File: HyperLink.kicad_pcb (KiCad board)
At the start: 2 copper layers, 35 x 24 mm, 45 parts, among them J1 USB_C_Receptacle_USB2.0, J2 Conn_02x05_Odd_Even, J3 Conn_02x05_Odd_Even, SW1 SW_Push, U1 ESP32-C3, U2 PESD2USB5UXT, U3 MIC5504-3.3YM5, Y1 ABM11W-40.0000MHZ-8-B1U-T3

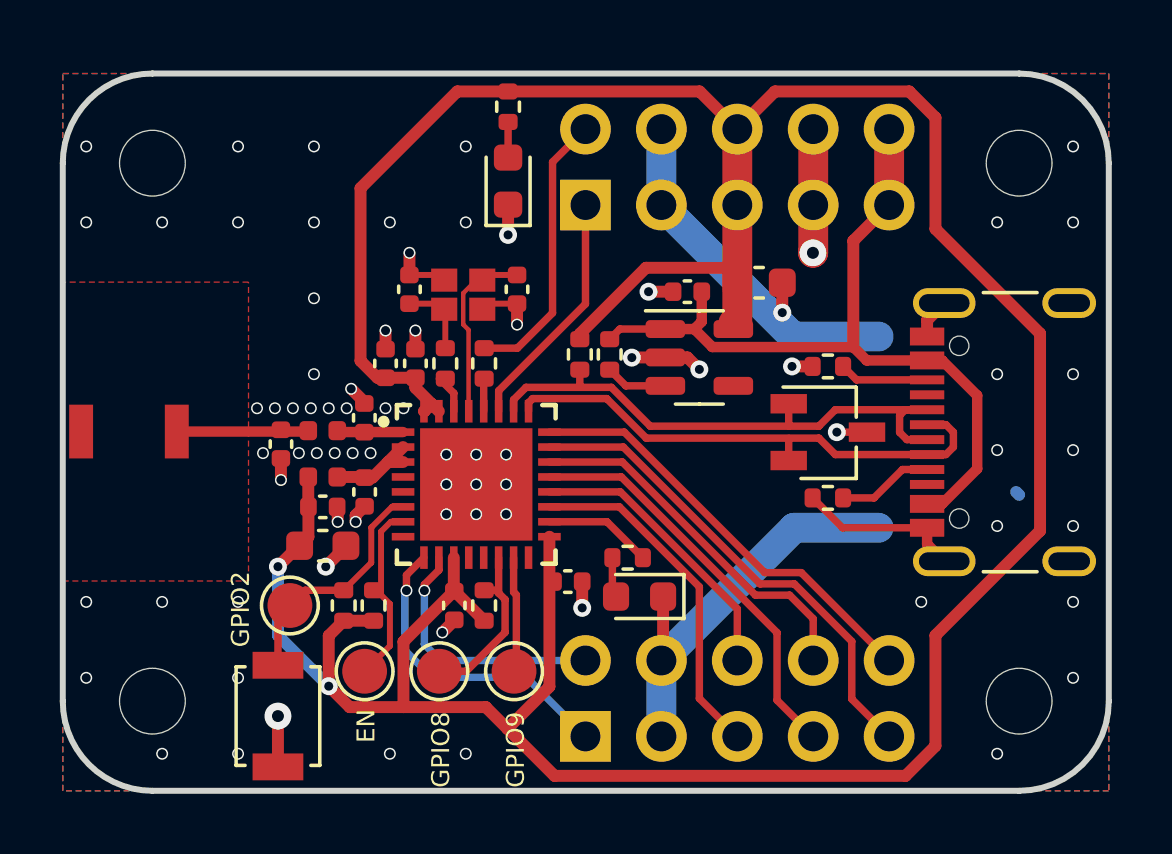
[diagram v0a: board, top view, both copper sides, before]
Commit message: Update crystal footprint
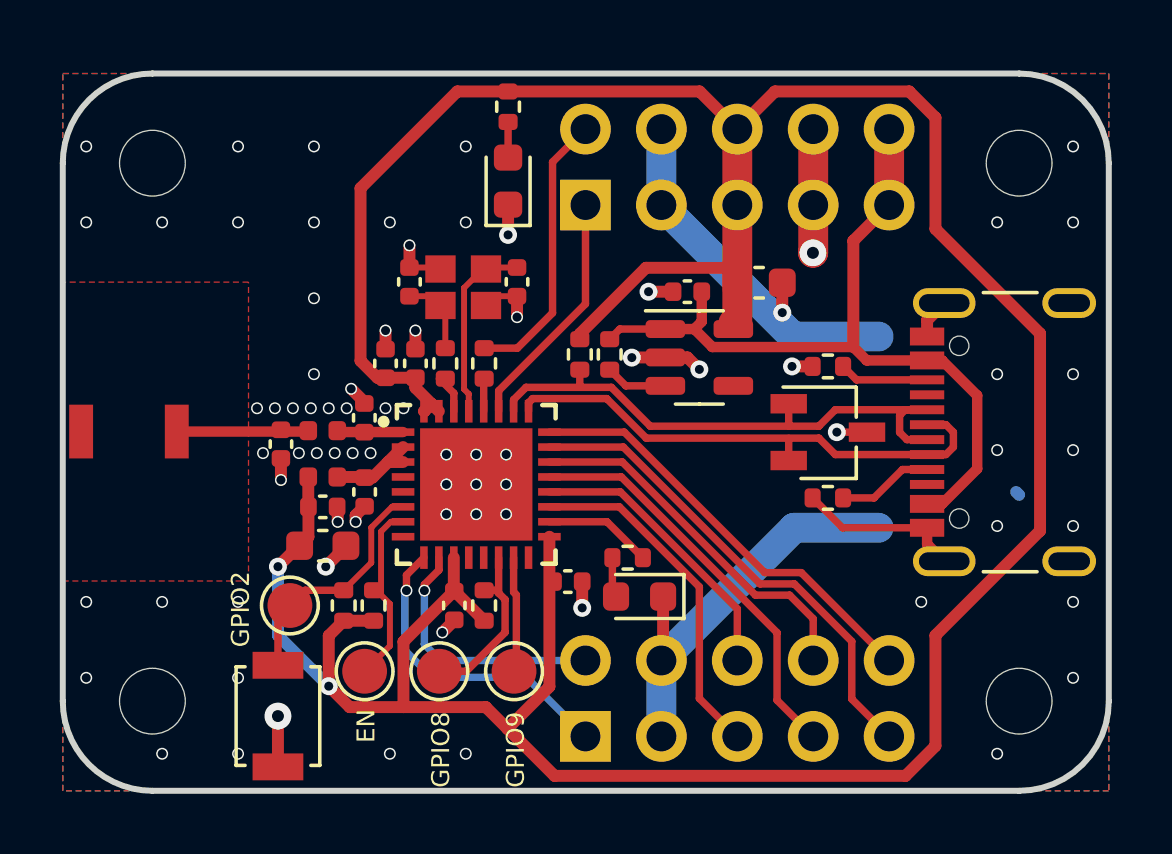
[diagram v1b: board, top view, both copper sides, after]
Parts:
- moved Y1 0.25 mm to (132.4, 77.2)
- moved C5 0.25 mm to (130.6, 77.0)
- moved C6 0.25 mm to (134.2, 77.0)
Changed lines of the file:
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@@
   )
   (footprint "Capacitor_SMD:C_0402_1005Metric" (layer "F.Cu")
-    (at 130.6 77.22 90)
+    (at 130.6 76.970999 90)
     (descr "Capacitor SMD 0402 (1005 Metric), square (rectangular) end terminal, IPC_7351 nominal, (Body size source: IPC-SM-782 page 76, https://www.pcb-3d.com/wordpress/wp-content/uploads/ipc-sm-782a_amendment_1_and_2.pdf), generated with kicad-footprint-generator")
     (tags "capacitor")
@@
   )
   (footprint "Capacitor_SMD:C_0402_1005Metric" (layer "F.Cu")
-    (at 134.2 77.22 -90)
+    (at 134.2 76.970999 -90)
     (descr "Capacitor SMD 0402 (1005 Metric), square (rectangular) end terminal, IPC_7351 nominal, (Body size source: IPC-SM-782 page 76, https://www.pcb-3d.com/wordpress/wp-content/uploads/ipc-sm-782a_amendment_1_and_2.pdf), generated with kicad-footprint-generator")
     (tags "capacitor")
@@
   )
   (footprint "encyclopedia_galactica:ABM11W-30.0000MHZ-7-D1X-T3" (layer "F.Cu")
-    (at 132.400001 77.4 180)
+    (at 132.400001 77.150999 180)
     (property "Sheetfile" "HyperLink.kicad_sch")
     (property "Sheetname" "")
     (property "ki_description" "Four pin crystal, GND on pins 2 and 3")
     (property "ki_keywords" "quartz ceramic resonator oscillator")
-    (clearance 0.1)
     (attr smd)
     (fp_text reference "Y1" (at 2.05 -2.16) (layer "F.SilkS") hide
@@
     (fp_line (start 1 -0.8) (end 1 0.8)
       (stroke (width 0.127) (type solid)) (layer "F.Fab"))
-    (pad "1" smd rect (at -0.637 -0.487 270) (size 0.775 0.875) (layers "F.Cu" "F.Paste" "F.Mask")
+    (pad "1" smd rect (at -0.762 -0.6096 270) (size 0.9144 1.016) (layers "F.Cu" "F.Paste" "F.Mask")
       (net 5 "GND") (pinfunction "1") (pintype "passive"))
-    (pad "2" smd rect (at 0.637 -0.487 270) (size 0.775 0.875) (layers "F.Cu" "F.Paste" "F.Mask")
+    (pad "2" smd rect (at 0.762 -0.6096 270) (size 0.9144 1.016) (layers "F.Cu" "F.Paste" "F.Mask")
       (net 20 "/XTAL_P") (pinfunction "2") (pintype "passive"))
-    (pad "3" smd rect (at -0.637 0.487 270) (size 0.775 0.875) (layers "F.Cu" "F.Paste" "F.Mask")
+    (pad "3" smd rect (at -0.762 0.6096 270) (size 0.9144 1.016) (layers "F.Cu" "F.Paste" "F.Mask")
       (net 21 "/XTAL_N") (pinfunction "3") (pintype "passive"))
-    (pad "4" smd rect (at 0.637 0.487 270) (size 0.775 0.875) (layers "F.Cu" "F.Paste" "F.Mask")
+    (pad "4" smd rect (at 0.762 0.6096 270) (size 0.9144 1.016) (layers "F.Cu" "F.Paste" "F.Mask")
       (net 5 "GND") (pinfunction "4") (pintype "passive"))
     (model "${KIPRJMOD}/encyclopedia_galactica/models/ABM11W-30.0000MHZ-7-D1X-T3.step"
@@
   (segment (start 128.2 84.52) (end 128.18 84.5) (width 0.4) (layer "F.Cu") (net 5))
   (segment (start 144.11 74.4) (end 144.11 71.86) (width 1) (layer "F.Cu") (net 5))
-  (segment (start 131.590001 76.74) (end 131.763001 76.913) (width 0.2) (layer "F.Cu") (net 5))
-  (segment (start 130.6 76.74) (end 131.590001 76.74) (width 0.2) (layer "F.Cu") (net 5))
+  (segment (start 131.590001 76.490999) (end 131.763001 76.663999) (width 0.2) (layer "F.Cu") (net 5))
+  (segment (start 130.6 76.490999) (end 131.590001 76.490999) (width 0.2) (layer "F.Cu") (net 5))
   (segment (start 143.075 78) (end 143.075 77) (width 0.4) (layer "F.Cu") (net 5))
   (segment (start 129.8 79.22) (end 129.8 78.6) (width 0.4) (layer "F.Cu") (net 5))
@@
   (segment (start 139.0875 87.5) (end 139.0875 89.5825) (width 0.4) (layer "F.Cu") (net 5))
   (segment (start 138.046557 79.5) (end 139.1625 79.5) (width 0.4) (layer "F.Cu") (net 5))
-  (segment (start 133.224001 77.7) (end 133.037001 77.887) (width 0.2) (layer "F.Cu") (net 5))
+  (segment (start 133.224001 77.450999) (end 133.037001 77.637999) (width 0.2) (layer "F.Cu") (net 5))
   (segment (start 139.0875 89.5825) (end 139.03 89.64) (width 0.4) (layer "F.Cu") (net 5))
   (segment (start 139.9 79.5) (end 139.1625 79.5) (width 0.4) (layer "F.Cu") (net 5))
   (segment (start 145.09 85.2) (end 147.92 85.2) (width 0.25) (layer "F.Cu") (net 5))
   (segment (start 128.475 85.825) (end 128.475 85.8) (width 0.4) (layer "F.Cu") (net 5))
-  (segment (start 134.2 78.4) (end 134.2 77.7) (width 0.4) (layer "F.Cu") (net 5))
+  (segment (start 134.2 78.150999) (end 134.2 77.450999) (width 0.4) (layer "F.Cu") (net 5))
   (segment (start 140.3 79.9) (end 139.9 79.5) (width 0.4) (layer "F.Cu") (net 5))
   (segment (start 136.38 87.88) (end 136.38 87) (width 0.4) (layer "F.Cu") (net 5))
-  (segment (start 130.6 76) (end 130.6 76.7) (width 0.4) (layer "F.Cu") (net 5))
+  (segment (start 130.6 75.750999) (end 130.6 76.450999) (width 0.4) (layer "F.Cu") (net 5))
   (segment (start 126.3 82.88) (end 126.3 83.6) (width 0.4) (layer "F.Cu") (net 5))
   (segment (start 127.8 86.5) (end 128.475 85.825) (width 0.4) (layer "F.Cu") (net 5))
   (segment (start 147.92 78.255) (end 148.495 77.68) (width 0.4) (layer "F.Cu") (net 5))
-  (segment (start 134.2 77.7) (end 133.224001 77.7) (width 0.2) (layer "F.Cu") (net 5))
+  (segment (start 134.2 77.450999) (end 133.224001 77.450999) (width 0.2) (layer "F.Cu") (net 5))
   (segment (start 138.040639 79.505918) (end 138.046557 79.5) (width 0.4) (layer "F.Cu") (net 5))
   (segment (start 144.11 74.4) (end 144.11 75.99) (width 1) (layer "F.Cu") (net 5))
@@
   (via (at 133.834851 84.7487) (size 0.4) (drill 0.3) (layers "F.Cu" "B.Cu") (net 5))
   (via (at 126.7 81.2) (size 0.4) (drill 0.3) (layers "F.Cu" "B.Cu") (free) (net 5))
-  (via (at 134.2 78.4) (size 0.4) (drill 0.3) (layers "F.Cu" "B.Cu") (free) (net 5))
+  (via (at 134.2 78.150999) (size 0.4) (drill 0.3) (layers "F.Cu" "B.Cu") (free) (net 5))
   (via (at 132.834851 83.7487) (size 0.4) (drill 0.3) (layers "F.Cu" "B.Cu") (net 5))
   (via (at 131.834851 84.7487) (size 0.4) (drill 0.3) (layers "F.Cu" "B.Cu") (net 5))
@@
   (via (at 132.834851 82.7487) (size 0.4) (drill 0.3) (layers "F.Cu" "B.Cu") (net 5))
   (via (at 124.865 74.979999) (size 0.4) (drill 0.3) (layers "F.Cu" "B.Cu") (free) (net 5))
-  (via (at 130.6 76) (size 0.4) (drill 0.3) (layers "F.Cu" "B.Cu") (free) (net 5))
+  (via (at 130.6 75.750999) (size 0.4) (drill 0.3) (layers "F.Cu" "B.Cu") (free) (net 5))
   (via (at 150.265 74.979999) (size 0.4) (drill 0.3) (layers "F.Cu" "B.Cu") (free) (net 5))
   (via (at 124.865 87.679999) (size 0.4) (drill 0.3) (layers "F.Cu" "B.Cu") (free) (net 5))
@@
   (segment (start 132.5 90) (end 133.8 88.7) (width 0.25) (layer "F.Cu") (net 19))
   (segment (start 133.8 87.6) (end 133.584852 87.384852) (width 0.25) (layer "F.Cu") (net 19))
-  (segment (start 131.8 79.19) (end 131.8 77.923999) (width 0.2) (layer "F.Cu") (net 20))
-  (segment (start 130.6 77.7) (end 131.576001 77.7) (width 0.2) (layer "F.Cu") (net 20))
-  (segment (start 131.576001 77.7) (end 131.763001 77.887) (width 0.2) (layer "F.Cu") (net 20))
-  (segment (start 131.8 77.923999) (end 131.763001 77.887) (width 0.2) (layer "F.Cu") (net 20))
-  (segment (start 134.2 76.74) (end 133.210001 76.74) (width 0.2) (layer "F.Cu") (net 21))
-  (segment (start 132.578 78.578) (end 132.4 78.4) (width 0.15) (layer "F.Cu") (net 21))
-  (segment (start 133.210001 76.74) (end 133.037001 76.913) (width 0.2) (layer "F.Cu") (net 21))
-  (segment (start 132.4 77.349001) (end 132.836001 76.913) (width 0.15) (layer "F.Cu") (net 21))
-  (segment (start 132.836001 76.913) (end 133.037001 76.913) (width 0.15) (layer "F.Cu") (net 21))
-  (segment (start 132.4 78.4) (end 132.4 77.349001) (width 0.15) (layer "F.Cu") (net 21))
-  (segment (start 132.584851 81.3) (end 132.578 81.293149) (width 0.15) (layer "F.Cu") (net 21))
-  (segment (start 132.578 81.293149) (end 132.578 78.578) (width 0.15) (layer "F.Cu") (net 21))
+  (segment (start 131.8 77.674998) (end 131.576001 77.450999) (width 0.2) (layer "F.Cu") (net 20))
+  (segment (start 131.8 79.19) (end 131.8 77.674998) (width 0.2) (layer "F.Cu") (net 20))
+  (segment (start 131.576001 77.450999) (end 130.6 77.450999) (width 0.2) (layer "F.Cu") (net 20))
+  (segment (start 132.427001 77.172999) (end 133.058601 76.541399) (width 0.2) (layer "F.Cu") (net 21))
+  (segment (start 132.427001 80.563551) (end 132.427001 77.172999) (width 0.2) (layer "F.Cu") (net 21))
+  (segment (start 134.2 76.490999) (end 133.212401 76.490999) (width 0.2) (layer "F.Cu") (net 21))
+  (segment (start 133.212401 76.490999) (end 133.162001 76.541399) (width 0.2) (layer "F.Cu") (net 21))
+  (segment (start 132.584851 81.3) (end 132.584851 80.721401) (width 0.2) (layer "F.Cu") (net 21))
+  (segment (start 132.584851 80.721401) (end 132.427001 80.563551) (width 0.2) (layer "F.Cu") (net 21))
+  (segment (start 133.058601 76.541399) (end 133.162001 76.541399) (width 0.2) (layer "F.Cu") (net 21))
   (segment (start 132.08485 80.69485) (end 131.6 80.21) (width 0.25) (layer "F.Cu") (net 22))
   (segment (start 132.08485 81.3) (end 132.08485 80.69485) (width 0.25) (layer "F.Cu") (net 22))

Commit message: Replace unnecessarily thick traces with thinner ones
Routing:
- net GND: track 55.5 -> 63.2 mm, vias 77 -> 76
- net +3V3: track 116.1 -> 116.9 mm

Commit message: Move status LED
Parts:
- moved D1 10.2 mm to (129.9, 93.2), turned to 0 degrees
- moved R11 9.56 mm to (130.3, 92.0), turned to 0 degrees
- moved D2 4.88 mm to (129.9, 70.8), turned to 0 degrees
- moved R12 3.71 mm to (130.3, 72.0), turned to 0 degrees
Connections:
- U1 pad 18: /STATUS_LED -> unconnected-(U1-VDD_SPI-Pad18)
- U1 pad 8: unconnected-(U1-GPIO3-Pad8) -> /STATUS_LED
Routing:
- net /STATUS_LED: track 3.62 -> 8.15 mm, vias 0 -> 2
- net GND: track 63.2 -> 62.3 mm
- net +3V3: track 116.9 -> 117.9 mm
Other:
- board text added: "HyperLink v1.1"
- board text added: "POWER"
- board text removed: "HyperLink v1.0"
